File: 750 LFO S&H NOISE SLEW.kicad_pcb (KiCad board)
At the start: 2 copper layers, 65 x 106.5 mm, 233 parts, among them J1 PJ301BM, J10 PJ301BM, J11 PJ301BM, J2 PJ301BM, J3 PJ301BM, J4 PJ301BM, J5 JACK_MONO_SW, J6 PJ301BM, J7 JACK_MONO_SW, J8 PJ301BM, J9 PJ301BM, P1 CONN_01X03, P3 CONN_02X05, Q1 MMBT3904, Q10 MMBT3904, Q11 J112, Q12 MMBT3906, Q13 J112, Q14 J112, Q15 MMBT3904, Q16 MMBT3904, Q2 MMBT3904, Q3 2N7002, Q4 2N7002, Q5 MBT3946DW, Q6 MBT3946DW, Q7 MMBT3904, Q8 MMBT3904, Q9 MMBT3904, SW1 KS-01Q, SW2 KS-01Q, SW3 SPDT, U1 LM13700, U10 TL072-, U11 TL072-, U12 MAX9945, U13 DG409, U14 DG409, U15 TS321, U2 TL072-, U3 TL072-, U4 TL072-, U5 TL072-, U6 CD40106, U7 CD4027, U8 CD4027, U9 TL072-

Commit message: working on v1.3. almost done
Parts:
- added C1: 0.1µ, MyModules:SM0603-C-JRL, B.Cu at (82.8, 90.7)
- added REF**: fiducial-1mm, MyModules:fiducial-1mm, B.Cu at (62.5, 129.2)
- added REF**: fiducial-1mm, MyModules:fiducial-1mm, B.Cu at (122.8, 27.2)
- R96, R97: value 2.2K -> 3.3K
- SW3: footprint MyModules:SS-12F45-1P2T-SLIDE -> MyModules:SS-12F108-1P2T-SLIDE
- VR1, VR6: value 100K B -> 100K
- VR4: value 1meg A -> 1meg
- VR8: value 1meg A -> 1meg LOG
- VR9: value 5K -> 10K
- moved R22 5.58 mm to (78.1, 92.4)
- moved TP3 3.09 mm to (123.2, 30.8)
- moved R4 2.17 mm to (110.4, 65.0), turned to 270 degrees
- moved C3 1.70 mm to (89.2, 102.5)
- moved R1 1.05 mm to (108.0, 65.0), turned to 90 degrees
- moved VR7 0.78 mm to (99.5, 67.4), turned to 180 degrees
- moved R3 0.75 mm to (89.2, 105.2)
- moved R66 0.67 mm to (96.0, 65.8), turned to 0 degrees
- moved R23 0.45 mm to (109.8, 91.0)
- moved Q8 0.35 mm to (112.4, 91.5)
- moved R2 0.32 mm to (81.3, 86.5)
- moved R31 0.30 mm to (115.2, 91.0)
- turned SW3 to 180 degrees
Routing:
- net GND: track 184.5 -> 217.7 mm, vias 39 -> 44
- net +12V: track 684.6 -> 653.4 mm, vias 38 -> 39
- net -12V: track 478.4 -> 470.2 mm
- net Net-(R1-Pad1): track 2.14 -> 9.61 mm
- net Net-(Q5-Pad1): track 3.91 -> 10.1 mm
- net Net-(R4-Pad1): track 26.8 -> 23.1 mm
- net Net-(R59-Pad2): track 61.2 -> 64.5 mm
- net LFO_SINE: track 140.2 -> 138.0 mm
- net Net-(R13-Pad1): track 47.4 -> 45.1 mm
- net Net-(D7-Pad2): track 89.4 -> 87.1 mm
- net LFO_TRI: track 112.6 -> 110.8 mm
- net Net-(C3-Pad1): track 12.0 -> 10.7 mm
- net Net-(C27-Pad1): track 30.4 -> 31.3 mm
- net Net-(J1-Pad3): track 40.8 -> 41.4 mm
- net Net-(Q5-Pad2): track 9.92 -> 10.5 mm
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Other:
- board text added: "v1.3 05 2017"
- board text removed: "v1.2 03 2017"

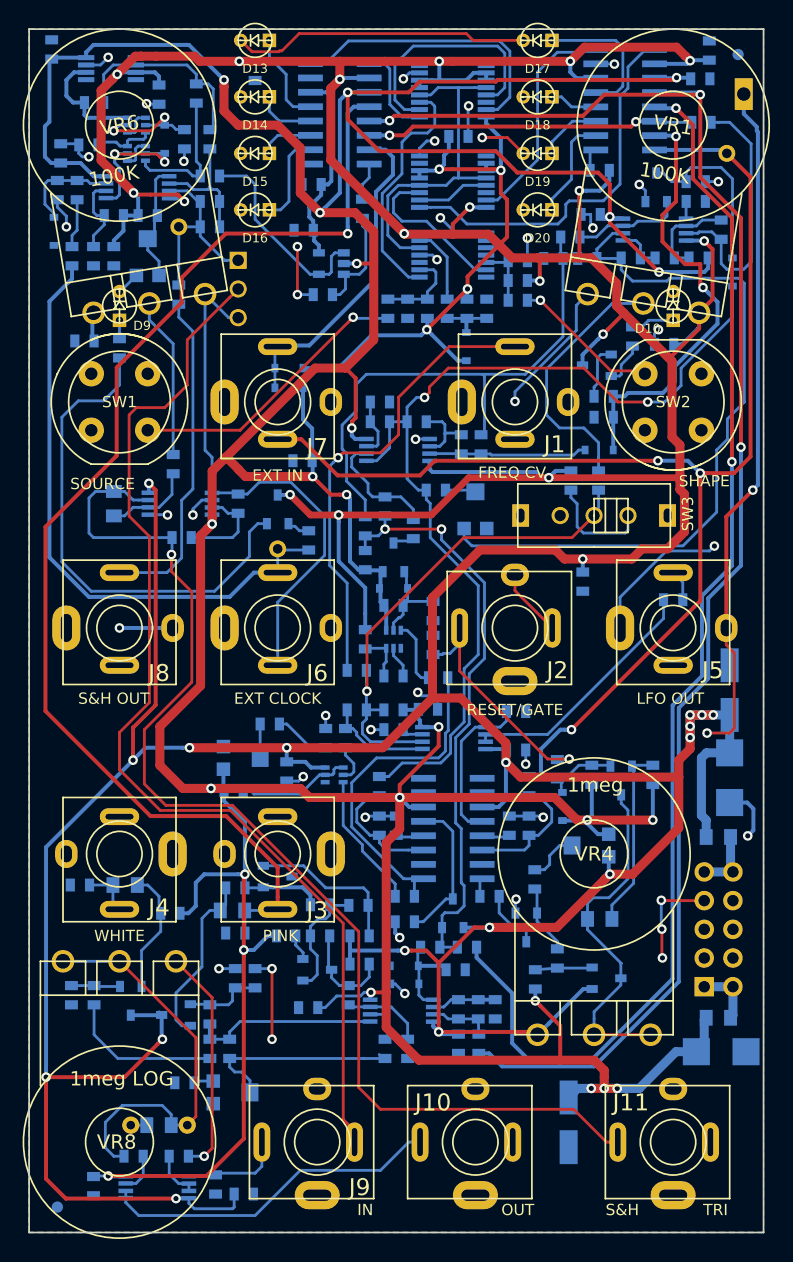
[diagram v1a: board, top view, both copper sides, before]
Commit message: added a couple of superflurous output protection resistors
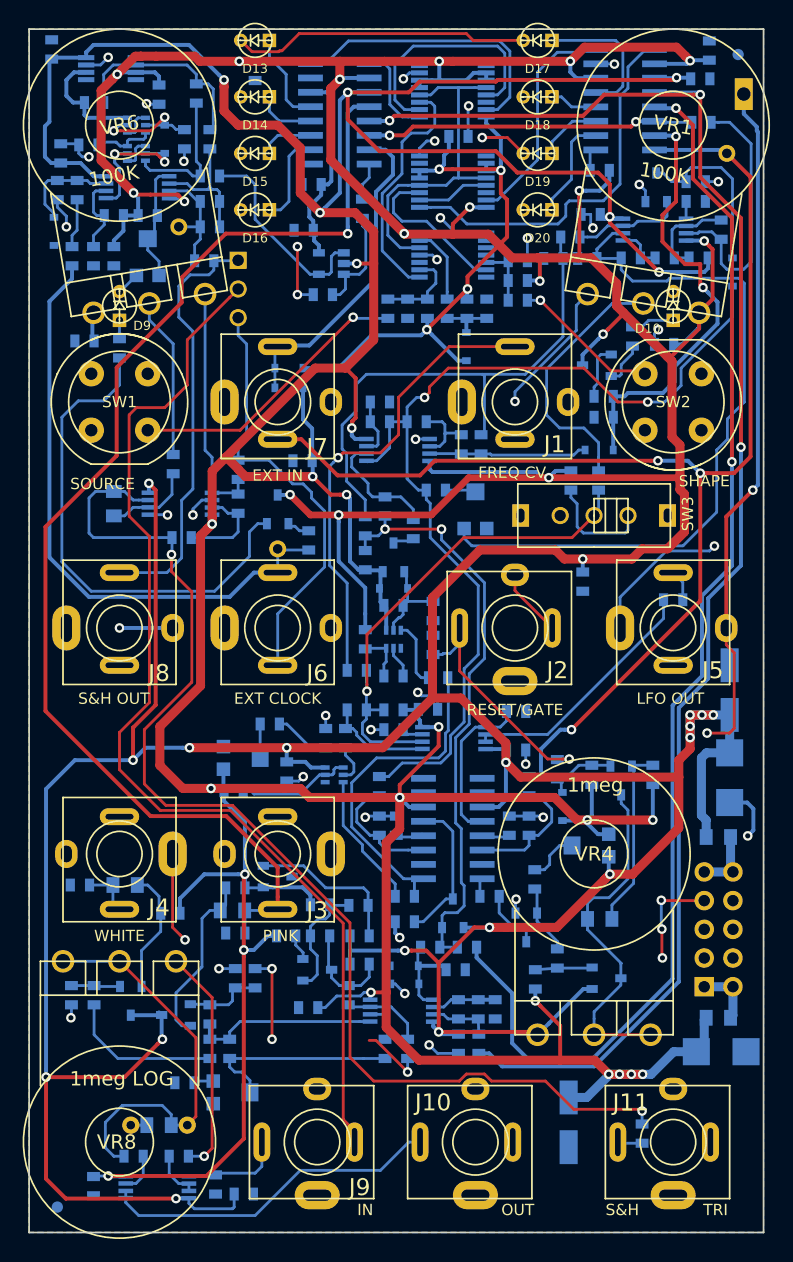
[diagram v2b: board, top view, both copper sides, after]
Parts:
- added G***: LOGO, LOGO, B.Cu at (112.2, 85.2)
- added R110: 1K, MyModules:SM0603-R-JRL, B.Cu at (78.5, 64.0)
- added R111: 1K, MyModules:SM0603-R-JRL, B.Cu at (114.2, 122.8)
- moved R99 3.75 mm to (75.5, 45.5), turned to 180 degrees
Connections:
- J11 pad 3: Net-(C34-Pad2) -> Net-(J11-Pad3)
- P1 pad 1: Net-(C37-Pad2) -> Net-(J8-Pad3)
- R56 pad 1: S&H_INT_CLK -> Net-(R110-Pad2)
- U9 pad 1: S&H_INT_CLK -> Net-(R110-Pad2)
- VR6 pad 3: S&H_INT_CLK -> Net-(R110-Pad2)
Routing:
- net Net-(R110-Pad2): track 0.00 -> 21.6 mm
- net GND: track 217.7 -> 235.6 mm, vias 44 -> 48
- net S&H_INT_CLK: track 48.3 -> 38.4 mm
- net Net-(J8-Pad3): track 29.5 -> 37.7 mm
- net Net-(C37-Pad2): track 17.6 -> 10.5 mm
- net +12V: track 653.4 -> 656.4 mm
- net Net-(J11-Pad3): track 0.00 -> 2.19 mm
- net Net-(C34-Pad2): track 103.9 -> 105.5 mm, vias 1 -> 2
- net -12V: track 470.2 -> 469.5 mm, vias 24 -> 25

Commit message: notes
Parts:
- R25: value 10K -> 22K
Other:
- board text removed: "SN#"
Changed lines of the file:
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@@
     (links 501)
     (no_connects 0)
-    (area 59.924999 24.924999 125.075001 131.575001)
+    (area 56.936905 22.45604 128.313095 132.325001)
     (thickness 1.6)
     (drawings 942)
@@
     (35 F.Paste user)
     (36 B.SilkS user)
-    (37 F.SilkS user)
+    (37 F.SilkS user hide)
     (38 B.Mask user)
     (39 F.Mask user)
@@
     (pad_to_mask_clearance 0.01)
     (aux_axis_origin 0 0)
-    (visible_elements 7FFFF77F)
+    (visible_elements 7FFFB7FF)
     (pcbplotparams
       (layerselection 0x010f0_80000001)
@@
       (effects (font (size 0.6096 0.6096) (thickness 0.1524)) (justify mirror))
     )
-    (fp_text value 2N7002 (at 1.016 -2.286 90) (layer B.SilkS) hide
+    (fp_text value 2N7002 (at -1.25 -0.5 90) (layer B.SilkS) hide
       (effects (font (size 0.8128 0.8128) (thickness 0.1524)) (justify mirror))
     )
@@
       (effects (font (size 0.6096 0.6096) (thickness 0.1524)) (justify mirror))
     )
-    (fp_text value 2N7002 (at 1.016 -2.286 90) (layer B.SilkS) hide
+    (fp_text value 2N7002 (at 1.2 0.05 90) (layer B.SilkS) hide
       (effects (font (size 0.8128 0.8128) (thickness 0.1524)) (justify mirror))
     )
@@
       (effects (font (size 0.6096 0.6096) (thickness 0.1524)) (justify mirror))
     )
-    (fp_text value 1N4148 (at 0 -1.905 90) (layer B.SilkS) hide
+    (fp_text value 1N4148 (at 0.15 -0.05 90) (layer B.SilkS) hide
       (effects (font (size 1 1) (thickness 0.15)) (justify mirror))
     )
@@
       (effects (font (size 0.6096 0.6096) (thickness 0.1524)) (justify mirror))
     )
-    (fp_text value 10K (at 0 0 270) (layer B.SilkS) hide
+    (fp_text value 22K (at 0 0 270) (layer B.SilkS) hide
       (effects (font (size 0.508 0.4572) (thickness 0.1143)) (justify mirror))
     )
@@
     (at 75.5 45.5 180)
     (attr smd)
-    (fp_text reference R99 (at -3 -0.75 180) (layer B.SilkS)
+    (fp_text reference R99 (at -0.1 -1.4 180) (layer B.SilkS)
       (effects (font (size 0.6096 0.6096) (thickness 0.1524)) (justify mirror))
     )
@@
     )
   )
-  (gr_text SN# (at 113.5 129.9) (layer B.SilkS)
-    (effects (font (size 1 1) (thickness 0.15)) (justify mirror))
-  )
+  (gr_line (start 63.45 66.9) (end 63.45 66.9) (angle 90) (layer B.SilkS) (width 5))
   (gr_line (start 109.4 128.3) (end 106.4 128.3) (angle 90) (layer B.SilkS) (width 5))
   (gr_text 850 (at 92.4 128.4) (layer B.SilkS)
@@
   (gr_line (start 68.000117 32.50286) (end 68.000117 34.50286) (layer Eco2.User) (width 0.1))
   (gr_text -12V (at 116.1 111.7) (layer B.SilkS)
-    (effects (font (size 1 1) (thickness 0.1524)) (justify mirror))
+    (effects (font (size 1.2 1.2) (thickness 0.25)) (justify mirror))
   )
   (gr_line (start 123.75 109.75) (end 116.25 109.75) (angle 90) (layer B.SilkS) (width 2))

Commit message: commit before adding voltage referencd for LFO
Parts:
- moved R26 0.56 mm to (66.2, 110.8)
- moved R29 0.56 mm to (64.2, 110.8)
- moved C44 0.35 mm to (71.2, 121.8), turned to 0 degrees
- moved Q9 0.25 mm to (69.0, 111.2)
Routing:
- net Net-(C44-Pad1): track 36.0 -> 28.3 mm
- net Net-(Q9-Pad1): track 4.57 -> 4.07 mm
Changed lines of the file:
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@@
     (thickness 1.6)
     (drawings 942)
-    (tracks 1971)
+    (tracks 1964)
     (zones 0)
     (modules 239)
@@
   )
   (module MyModules:SOT23-132-JRL (layer B.Cu)
-    (at 69 111)
+    (at 69 111.25)
     (tags SOT23)
     (fp_text reference Q9 (at 1.99898 0.09906 270) (layer B.SilkS)
@@
   )
   (module MyModules:SM0603-R-JRL (layer B.Cu)
-    (at 65.75 110.5 90)
+    (at 66.25 110.75 90)
     (attr smd)
     (fp_text reference R26 (at 2 0 180) (layer B.SilkS)
@@
   )
   (module MyModules:SM0603-R-JRL (layer B.Cu)
-    (at 63.75 110.5 270)
+    (at 64.25 110.75 270)
     (attr smd)
     (fp_text reference R29 (at 0 1.4 270) (layer B.SilkS)
@@
   )
   (module MyModules:CAP-5MM-BOX-0805-COMBO (layer B.Cu)
-    (at 71.5 122 180)
-    (fp_text reference C44 (at 4.4 0 270) (layer B.SilkS)
+    (at 71.25 121.75)
+    (fp_text reference C44 (at 4.4 0 90) (layer B.SilkS)
       (effects (font (size 0.8128 0.8128) (thickness 0.1524)) (justify mirror))
     )
-    (fp_text value 470n (at 1.6 2.6 180) (layer B.Fab) hide
+    (fp_text value 470n (at 1.6 2.6) (layer B.Fab) hide
       (effects (font (size 1 1) (thickness 0.15)) (justify mirror))
     )
@@
     (fp_line (start -1.75 0.75) (end -1.75 -0.75) (layer B.SilkS) (width 0.15))
     (fp_line (start 1.75 0.75) (end 1.75 -0.75) (layer B.SilkS) (width 0.15))
-    (pad 1 thru_hole circle (at -2.5 0 180) (size 1.524 1.524) (drill 0.762) (layers *.Cu *.Mask B.SilkS)
+    (pad 1 thru_hole circle (at -2.5 0) (size 1.524 1.524) (drill 0.762) (layers *.Cu *.Mask B.SilkS)
       (net 35 "Net-(C44-Pad1)"))
-    (pad 2 thru_hole circle (at 2.5 0 180) (size 1.524 1.524) (drill 0.762) (layers *.Cu *.Mask B.SilkS)
+    (pad 2 thru_hole circle (at 2.5 0) (size 1.524 1.524) (drill 0.762) (layers *.Cu *.Mask B.SilkS)
       (net 1 GND))
-    (pad 1 smd rect (at -1.0795 0 180) (size 1.143 1.397) (layers B.Cu B.Paste B.Mask)
+    (pad 1 smd rect (at -1.0795 0) (size 1.143 1.397) (layers B.Cu B.Paste B.Mask)
       (net 35 "Net-(C44-Pad1)"))
-    (pad 2 smd rect (at 1.0795 0 180) (size 1.143 1.397) (layers B.Cu B.Paste B.Mask)
+    (pad 2 smd rect (at 1.0795 0) (size 1.143 1.397) (layers B.Cu B.Paste B.Mask)
       (net 1 GND))
   )
@@
   (gr_line (start 125 25) (end 125 131.5) (angle 90) (layer Edge.Cuts) (width 0.15))
   (gr_line (start 60 25) (end 125 25) (angle 90) (layer Edge.Cuts) (width 0.15))
+  (segment (start 64.25 111.6009) (end 64.25 112.75) (width 0.25) (layer B.Cu) (net 1))
+  (via (at 64.25 112.75) (size 0.85) (drill 0.45) (layers F.Cu B.Cu) (net 1))
+  (segment (start 72.3295 121.75) (end 73.75 121.75) (width 0.25) (layer B.Cu) (net 1))
   (segment (start 93.5 117.3) (end 90.7 114.5) (width 0.25) (layer F.Cu) (net 1))
   (segment (start 90.7 114.5) (end 90.1 114.5) (width 0.25) (layer F.Cu) (net 1))
@@
   (segment (start 96.1509 115.6509) (end 95.4 114.9) (width 0.25) (layer B.Cu) (net 1))
   (via (at 95.4 114.9) (size 0.85) (drill 0.45) (layers F.Cu B.Cu) (net 1))
-  (segment (start 63.75 111.3509) (end 63.75 112.45) (width 0.25) (layer B.Cu) (net 1))
-  (segment (start 63.75 112.45) (end 63.7 112.5) (width 0.25) (layer B.Cu) (net 1))
-  (via (at 63.7 112.5) (size 0.85) (drill 0.45) (layers F.Cu B.Cu) (net 1))
   (segment (start 73.375001 105.175001) (end 73.8 105.6) (width 0.25) (layer F.Cu) (net 1))
   (segment (start 72.7 104.5) (end 73.375001 105.175001) (width 0.25) (layer F.Cu) (net 1))
@@
   (segment (start 114.5475 39.2975) (end 114 38.75) (width 0.25) (layer B.Cu) (net 1))
   (via (at 114 38.75) (size 0.85) (drill 0.45) (layers F.Cu B.Cu) (net 1))
-  (segment (start 70.4205 122) (end 69 122) (width 0.25) (layer B.Cu) (net 1))
   (segment (start 110.15158 28.075) (end 111.775 28.075) (width 0.25) (layer B.Cu) (net 1))
   (segment (start 111.775 28.075) (end 111.8 28.1) (width 0.25) (layer B.Cu) (net 1))
@@
   (segment (start 90.05 105.1991) (end 90.05 102.5991) (width 0.25) (layer B.Cu) (net 3))
   (segment (start 90.05 102.5991) (end 90.0009 102.55) (width 0.25) (layer B.Cu) (net 3))
+  (segment (start 69 112.52) (end 69.27 112.25) (width 0.35) (layer B.Cu) (net 4))
+  (segment (start 69.27 112.25) (end 71.73 112.25) (width 0.35) (layer B.Cu) (net 4))
   (segment (start 69.2 89.699998) (end 64.050002 89.699998) (width 0.35) (layer B.Cu) (net 4))
   (segment (start 64.050002 89.699998) (end 61.5 92.25) (width 0.35) (layer B.Cu) (net 4))
@@
   (segment (start 61.5 126.5) (end 61.5 117.75) (width 0.35) (layer F.Cu) (net 4))
   (via (at 61.5 117.75) (size 0.85) (drill 0.45) (layers F.Cu B.Cu) (net 4))
-  (segment (start 69 112.27) (end 71.71 112.27) (width 0.35) (layer B.Cu) (net 4))
-  (segment (start 71.71 112.27) (end 71.73 112.25) (width 0.35) (layer B.Cu) (net 4))
   (segment (start 95.7 83) (end 95.7 75.3) (width 0.8) (layer F.Cu) (net 4))
   (segment (start 95.7 75.3) (end 99.9 71.1) (width 0.8) (layer F.Cu) (net 4))
@@
   (segment (start 118.5 88.7) (end 118.5 85.7) (width 0.8) (layer F.Cu) (net 4))
   (via (at 118.5 85.7) (size 0.85) (drill 0.45) (layers F.Cu B.Cu) (net 4))
-  (segment (start 71.5 112.02) (end 71.73 112.25) (width 0.35) (layer B.Cu) (net 4))
   (segment (start 88.3991 106.9) (end 88.3991 107.75) (width 0.35) (layer B.Cu) (net 4))
   (segment (start 100.45 28.875) (end 99.35 28.875) (width 0.35) (layer B.Cu) (net 4))
@@
   (segment (start 80 109.8509) (end 78.25 109.8509) (width 0.25) (layer B.Cu) (net 12))
   (segment (start 76 116.1009) (end 67.8509 116.1009) (width 0.25) (layer B.Cu) (net 13))
-  (segment (start 67.8509 116.1009) (end 65.75 114) (width 0.25) (layer B.Cu) (net 13))
-  (segment (start 65.75 114) (end 65.75 111.3509) (width 0.25) (layer B.Cu) (net 13))
+  (segment (start 67.8509 116.1009) (end 66.25 114.5) (width 0.25) (layer B.Cu) (net 13))
+  (segment (start 66.25 114.5) (end 66.25 111.6009) (width 0.25) (layer B.Cu) (net 13))
   (segment (start 77.75 114.3991) (end 77.75 113.75) (width 0.25) (layer B.Cu) (net 14))
   (segment (start 77.75 113.75) (end 78.6696 112.8304) (width 0.25) (layer B.Cu) (net 14))
@@
   (segment (start 69.9525 106.5475) (end 71.6491 104.8509) (width 0.25) (layer B.Cu) (net 20))
   (segment (start 71.6491 104.8509) (end 71.6491 103.25) (width 0.25) (layer B.Cu) (net 20))
-  (segment (start 69.9525 109.73) (end 69.9525 106.5475) (width 0.25) (layer B.Cu) (net 20))
+  (segment (start 69.9525 109.98) (end 69.9525 106.5475) (width 0.25) (layer B.Cu) (net 20) (status 10))
   (segment (start 97.5 101.98) (end 96.89948 101.98) (width 0.25) (layer B.Cu) (net 21))
   (segment (start 96.89948 101.98) (end 94.87948 104) (width 0.25) (layer B.Cu) (net 21))
@@
   (segment (start 98.75 50.6009) (end 100.5 50.6009) (width 0.25) (layer B.Cu) (net 34))
   (segment (start 97 50.6009) (end 98.75 50.6009) (width 0.25) (layer B.Cu) (net 34))
-  (segment (start 74 122) (end 74.761999 121.238001) (width 0.25) (layer F.Cu) (net 35))
-  (segment (start 74.761999 121.238001) (end 74.761999 114.261999) (width 0.25) (layer F.Cu) (net 35))
-  (segment (start 74.761999 114.261999) (end 68 107.5) (width 0.25) (layer F.Cu) (net 35))
+  (segment (start 68.75 121.75) (end 73.75 116.75) (width 0.25) (layer F.Cu) (net 35))
+  (segment (start 73.75 116.75) (end 73.75 113.25) (width 0.25) (layer F.Cu) (net 35))
+  (segment (start 73.75 113.25) (end 68 107.5) (width 0.25) (layer F.Cu) (net 35))
+  (segment (start 68.3991 124.75) (end 68.3991 122.1009) (width 0.25) (layer B.Cu) (net 35))
+  (segment (start 68.3991 122.1009) (end 68.75 121.75) (width 0.25) (layer B.Cu) (net 35))
+  (segment (start 70.1705 121.75) (end 68.75 121.75) (width 0.25) (layer B.Cu) (net 35))
   (segment (start 68 107.5) (end 63 107.5) (width 0.25) (layer B.Cu) (net 35))
-  (segment (start 72.5795 122) (end 74 122) (width 0.25) (layer B.Cu) (net 35))
-  (segment (start 72.5795 122) (end 72.5795 121.0515) (width 0.25) (layer B.Cu) (net 35))
-  (segment (start 67.5 124.75) (end 68.3991 124.75) (width 0.25) (layer B.Cu) (net 35))
-  (segment (start 72.5795 121.0515) (end 71.778 120.25) (width 0.25) (layer B.Cu) (net 35))
-  (segment (start 71.778 120.25) (end 68.25 120.25) (width 0.25) (layer B.Cu) (net 35))
-  (segment (start 68.25 120.25) (end 66.75 121.75) (width 0.25) (layer B.Cu) (net 35))
-  (segment (start 66.75 121.75) (end 66.75 124) (width 0.25) (layer B.Cu) (net 35))
-  (segment (start 66.75 124) (end 67.5 124.75) (width 0.25) (layer B.Cu) (net 35))
   (segment (start 94.4446 107.9) (end 94.4 107.8554) (width 0.25) (layer B.Cu) (net 36))
   (segment (start 94.4 107.8554) (end 94.4 106.4991) (width 0.25) (layer B.Cu) (net 36))
@@
   (segment (start 91.3991 81.2009) (end 91.3991 82.25) (width 0.25) (layer B.Cu) (net 78))
   (segment (start 91.6023 79.79756) (end 91.6023 80.9977) (width 0.25) (layer B.Cu) (net 78))
-  (segment (start 68.0475 109.73) (end 65.8309 109.73) (width 0.25) (layer B.Cu) (net 79))
-  (segment (start 65.8309 109.73) (end 65.75 109.6491) (width 0.25) (layer B.Cu) (net 79))
-  (segment (start 65.9191 109.48) (end 65.75 109.6491) (width 0.25) (layer B.Cu) (net 79) (status 30))
-  (segment (start 63.75 109.6491) (end 65.75 109.6491) (width 0.25) (layer B.Cu) (net 79) (status 20))
+  (segment (start 68.0475 109.98) (end 66.3309 109.98) (width 0.25) (layer B.Cu) (net 79) (status 10))
+  (segment (start 66.3309 109.98) (end 66.25 109.8991) (width 0.25) (layer B.Cu) (net 79) (status 30))
+  (segment (start 66.4191 109.73) (end 66.25 109.8991) (width 0.25) (layer B.Cu) (net 79) (status 30))
+  (segment (start 64.25 109.8991) (end 66.25 109.8991) (width 0.25) (layer B.Cu) (net 79) (status 10))
   (segment (start 92.25 70.48) (end 92.43 70.3) (width 0.25) (layer B.Cu) (net 80))
   (segment (start 92.43 70.3) (end 93.8009 70.3) (width 0.25) (layer B.Cu) (net 80))

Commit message: LFO voltage reference added and routed"
l
q
;ksadjf

q
exit
"
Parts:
- removed R41: 10, MyModules:SM0805-HAND
- added C2: 1000p, MyModules:SM0603-C-JRL, B.Cu at (84.8, 67.2)
- added D24: LM4040-10, MyModules:SOT23-132-JRL, B.Cu at (73.0, 91.3)
- added F1: PTC 0.1A, Capacitors_SMD:C_0805, B.Cu at (121.0, 96.4)
- added F2: PTC 0.1A, Capacitors_SMD:C_0805, B.Cu at (120.8, 112.5)
- D3, D4: value D -> S1BB
- R1: value 270K -> 180K
- R40: value 10 -> 1K; footprint MyModules:SM0805-HAND -> MyModules:SM0603-R-JRL
- R72: value 330K -> 150K
- R8: value 150K -> 120K
- moved R40 47.9 mm to (73.1, 94.4)
- moved R1 5.55 mm to (113.5, 65.0)
- moved C1 1.14 mm to (83.9, 91.0)
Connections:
- C1 pad 1: +12V -> +10V
- P3 pad 10: Net-(P3-Pad10) -> Net-(F1-Pad1)
- P3 pad 9: Net-(P3-Pad10) -> Net-(F1-Pad1)
- Q5 pad 6: +12V -> +10V
- R1 pad 2: +12V -> +10V
- R40 pad 2: Net-(P3-Pad10) -> +10V
- VR1 pad 3: +12V -> +10V
- VR3 pad 3: +12V -> +10V
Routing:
- net +10V: track 0.00 -> 97.2 mm, vias 0 -> 3
- net GND: track 235.5 -> 268.3 mm, vias 48 -> 51
- net Net-(R1-Pad1): track 9.61 -> 2.41 mm
- net Net-(P3-Pad10): track 5.72 -> 0.00 mm
- net Net-(F1-Pad1): track 0.00 -> 5.72 mm
- net +12V: track 656.2 -> 650.7 mm
- net Net-(D7-Pad2): track 87.1 -> 89.2 mm
- net LFO_PULSE: track 39.2 -> 37.4 mm
- net Net-(C2-Pad1): track 2.06 -> 3.43 mm
- net S&H_INT_CLK: track 38.4 -> 39.0 mm
